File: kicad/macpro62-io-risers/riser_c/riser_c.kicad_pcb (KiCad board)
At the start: 4 copper layers, 16.8 x 34.2 mm, 14 parts, among them J1 C1 SHOU HAN TYPE-C 24PLT-H10.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, J10 DF40C-80DS-0.4V(51) C312960 r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, J2 C2 SHOU HAN TYPE-C 24PLT-H10.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, J3 C3 SHOU HAN TYPE-C 24PLT-H10.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

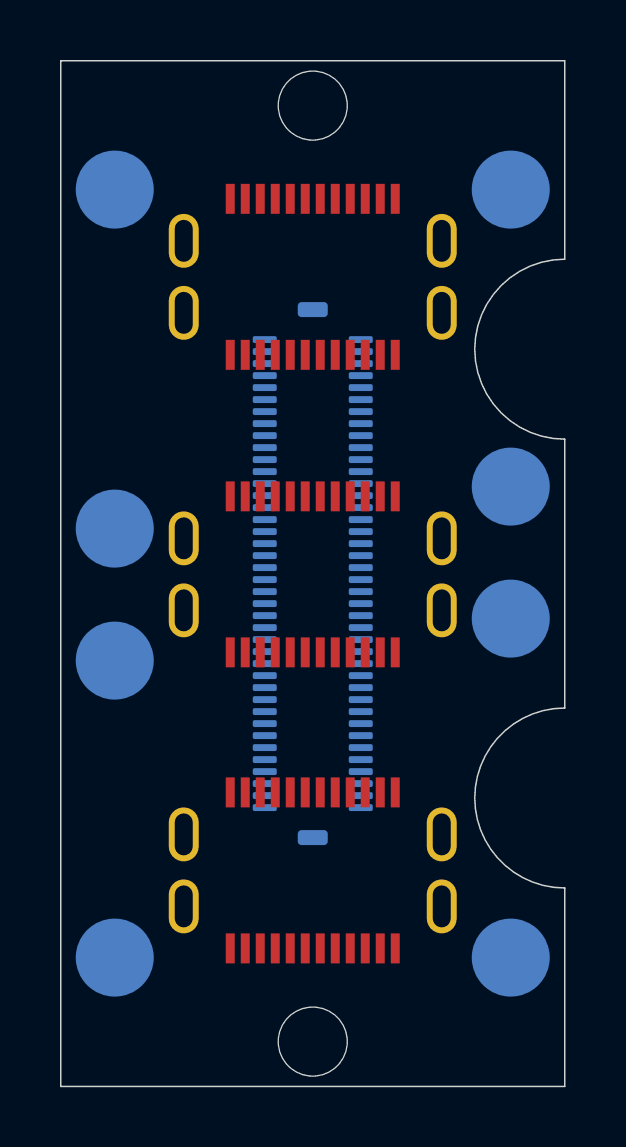
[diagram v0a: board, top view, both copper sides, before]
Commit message: I/O: ports tilted 12.5 deg per stock, riser edge trims, USB-A B2B moved on top, outer-face plug seats, D21-D26 removed
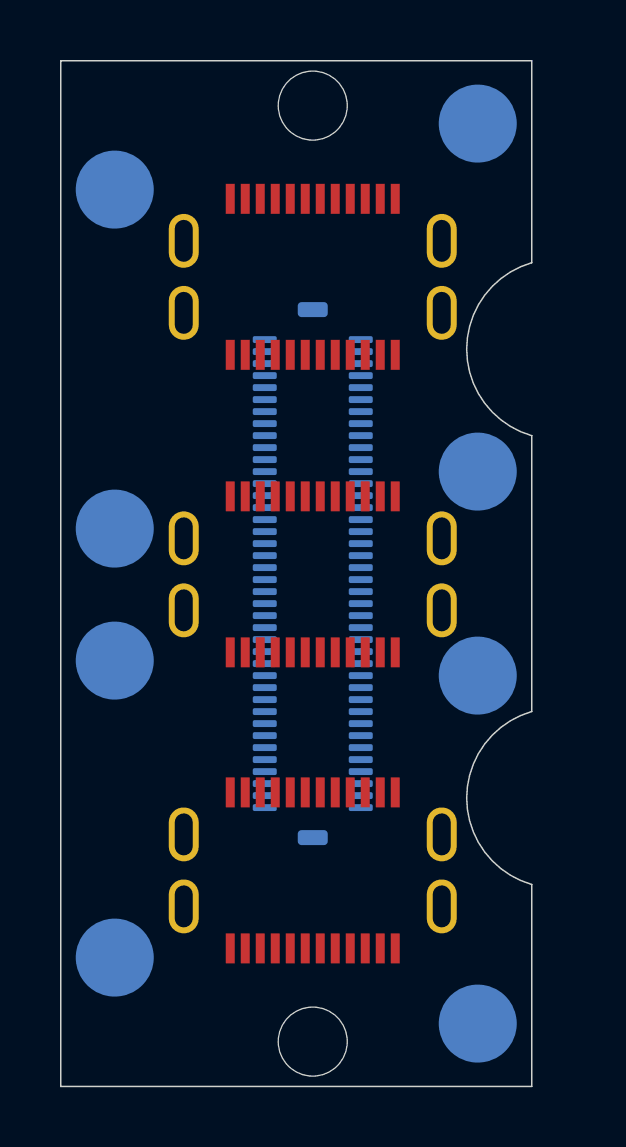
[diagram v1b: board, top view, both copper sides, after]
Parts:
- J1: value C1 SHOU HAN TYPE-C 24PLT-H10.5 (C3151750) (mouth 18.59 above main board top) -> C1 SHOU HAN TYPE-C 24PLT-H10.5 (C3151750) (mouth 18.03 above main board top)
- J2: value C2 SHOU HAN TYPE-C 24PLT-H10.5 (C3151750) (mouth 18.59 above main board top) -> C2 SHOU HAN TYPE-C 24PLT-H10.5 (C3151750) (mouth 18.03 above main board top)
- J3: value C3 SHOU HAN TYPE-C 24PLT-H10.5 (C3151750) (mouth 18.59 above main board top) -> C3 SHOU HAN TYPE-C 24PLT-H10.5 (C3151750) (mouth 18.03 above main board top)
- moved TP2 2.46 mm to (105.5, 115.0)
- moved TP6 2.46 mm to (105.5, 85.0)
- moved TP4 2.20 mm to (105.5, 103.4)
- moved TP8 1.21 mm to (105.5, 96.6)
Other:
- board size 16.8 x 34.2 mm -> 15.7 x 34.2 mm
- board text added: "riser_c A0 12.5 deg"
- board text removed: "riser_c A0 5.3 deg"
